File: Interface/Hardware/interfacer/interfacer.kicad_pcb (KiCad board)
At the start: 2 copper layers, 125.5 x 56.9 mm, 103 parts, among them J1 I2C, J10 5VDC barrel jack, J11 PWR, J12 5V, J13 GPS2 conn, J14 PPS direct, J15 PPS feedback, J16 DC/DC in, J17 5V isolated, J18 RJ45, J19 left top conn, J2 line UART, J20 right top conn, J3 GPS2 UART, J4 GPS1 UART, J5 PPS direct, J6 PPS selecctor, J7 PPS feedback, J8 left bottom conn, J9 right bottom conn, Q1 BSV52LT1G, Q2 BSV52LT1G, U1 ULN2003A, U2 LM92, U3 LM2940S-5.0, U4 L86, U5 NXJ1S0505MC, U6 ISO7421E, U7 ISO7421E, U8 SN65LBC179A, U9 SN65LBC179A

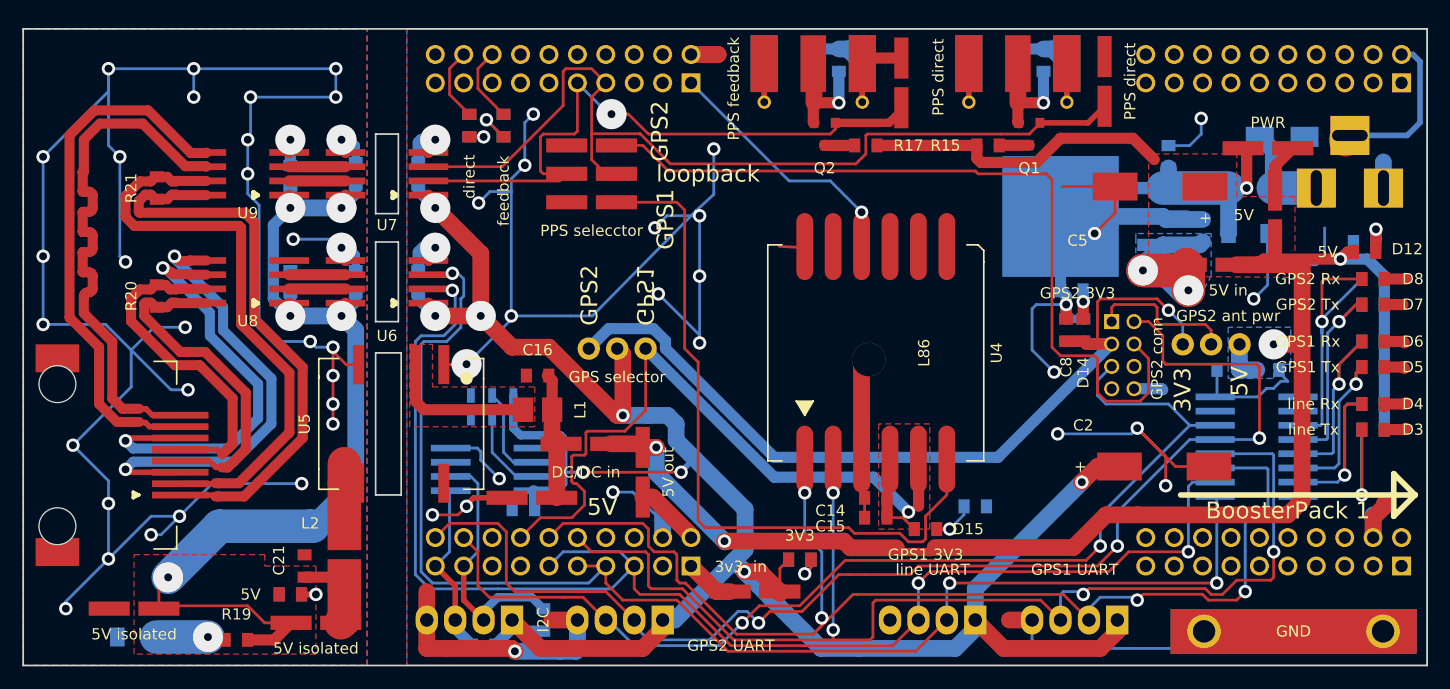
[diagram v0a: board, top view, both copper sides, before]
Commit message: silkscreen and solder mask finalization wiring touch-up
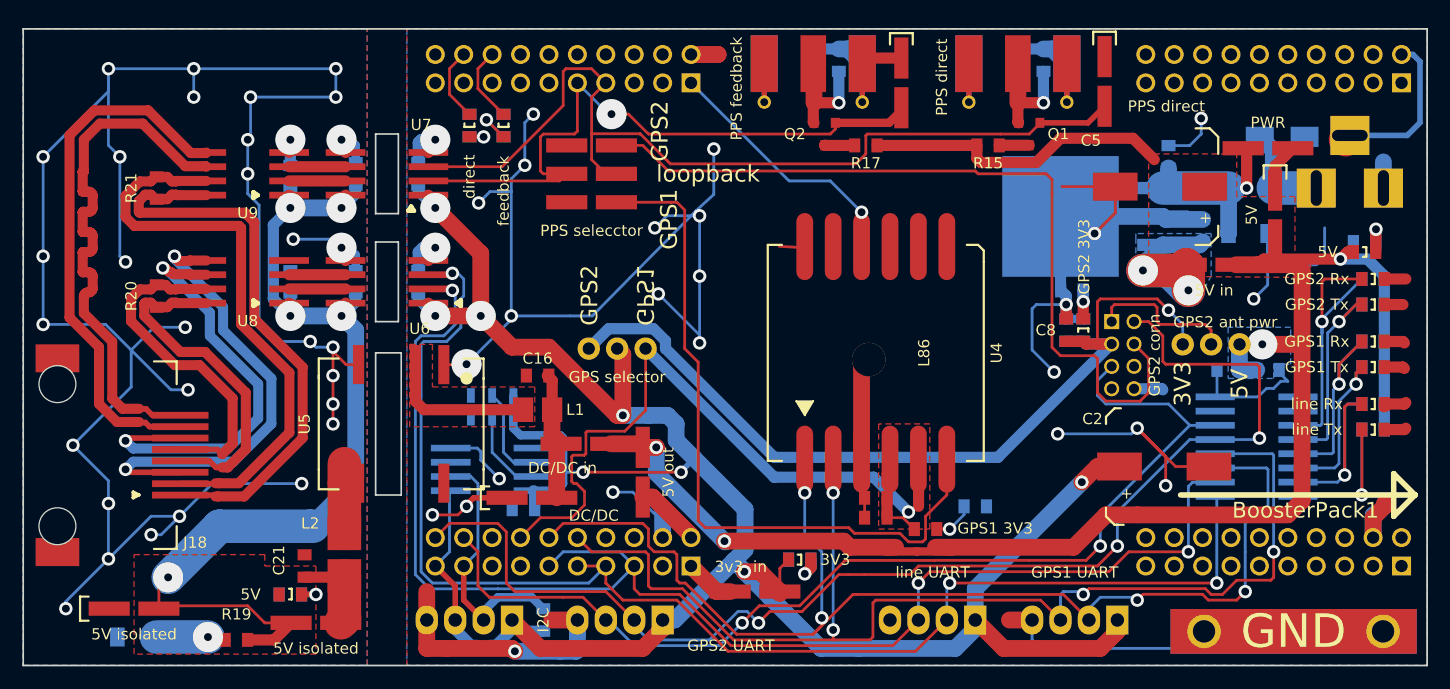
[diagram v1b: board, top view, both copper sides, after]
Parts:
- J16: value DC/DC in -> DC/DC
- J18: footprint auxiliary:8P8C_SMD -> 8P8C_SMD
- U4: footprint auxiliary:L86 -> L86
- moved R1 0.10 mm to (127.5, 125.3)
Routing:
- net +5V: track 157.3 -> 160.5 mm
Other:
- rule solder_mask_min_width: 0.16 -> 0.2
- board text added: "6.5V-20V"
- board text added: "BoosterPack1"
- board text removed: "BoosterPack 1"

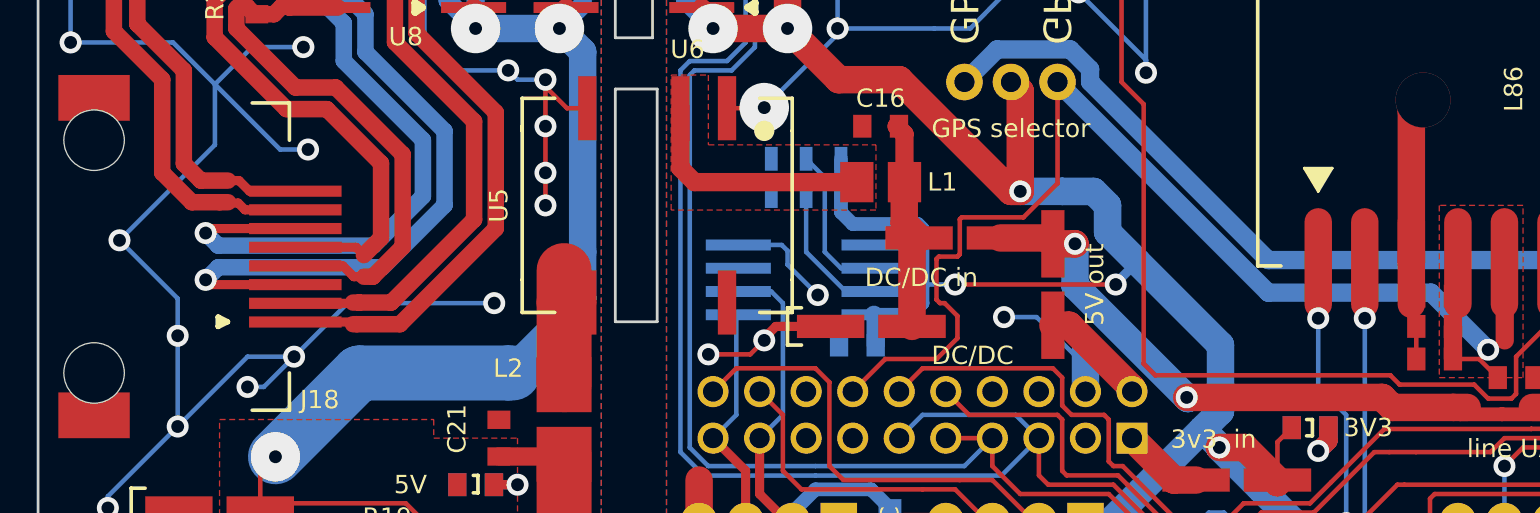
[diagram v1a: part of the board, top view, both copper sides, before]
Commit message: 8P8C, GPS1 gnd pin fix
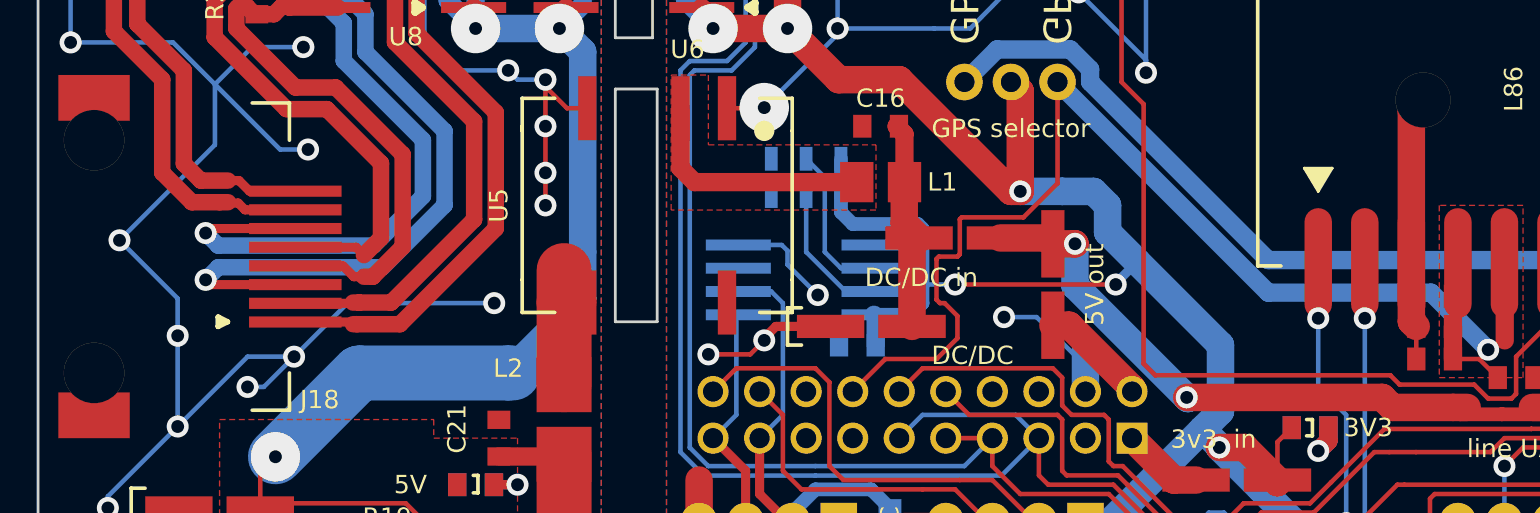
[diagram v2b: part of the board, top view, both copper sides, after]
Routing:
- net GND: track 396.2 -> 399.8 mm

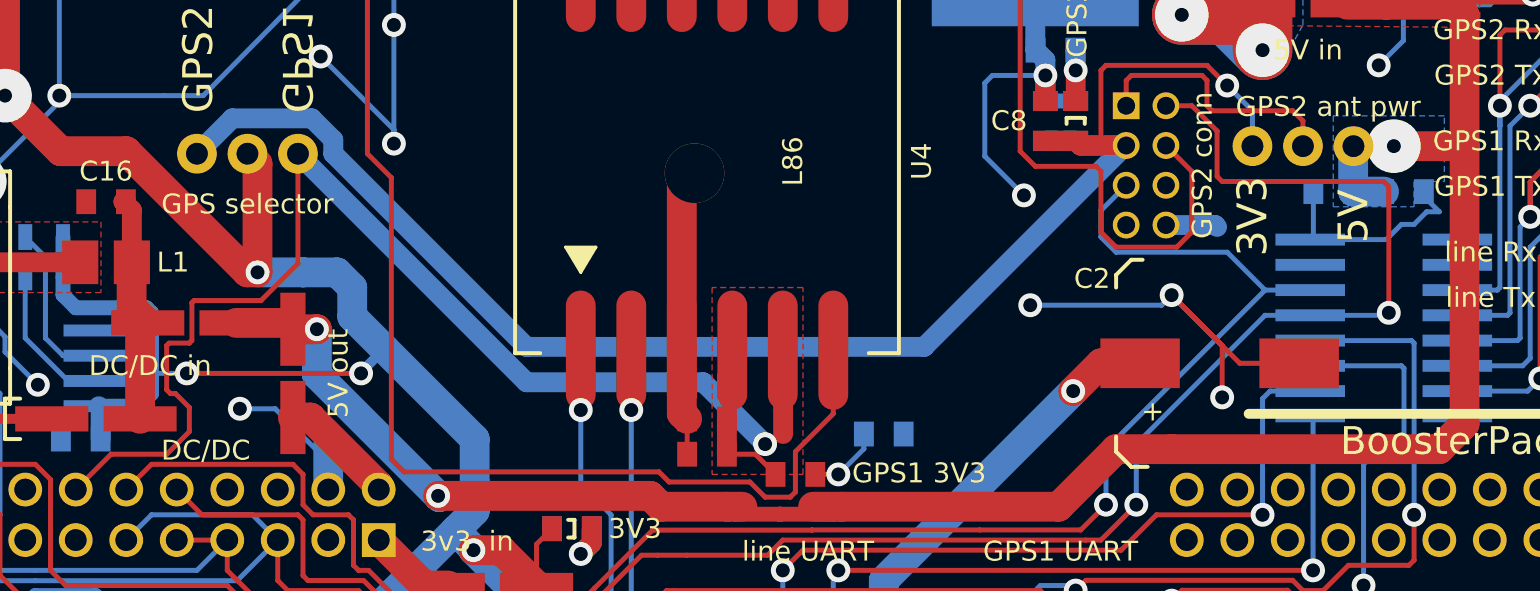
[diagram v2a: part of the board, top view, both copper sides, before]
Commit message: antenna power touch-up & green LED resistor value change
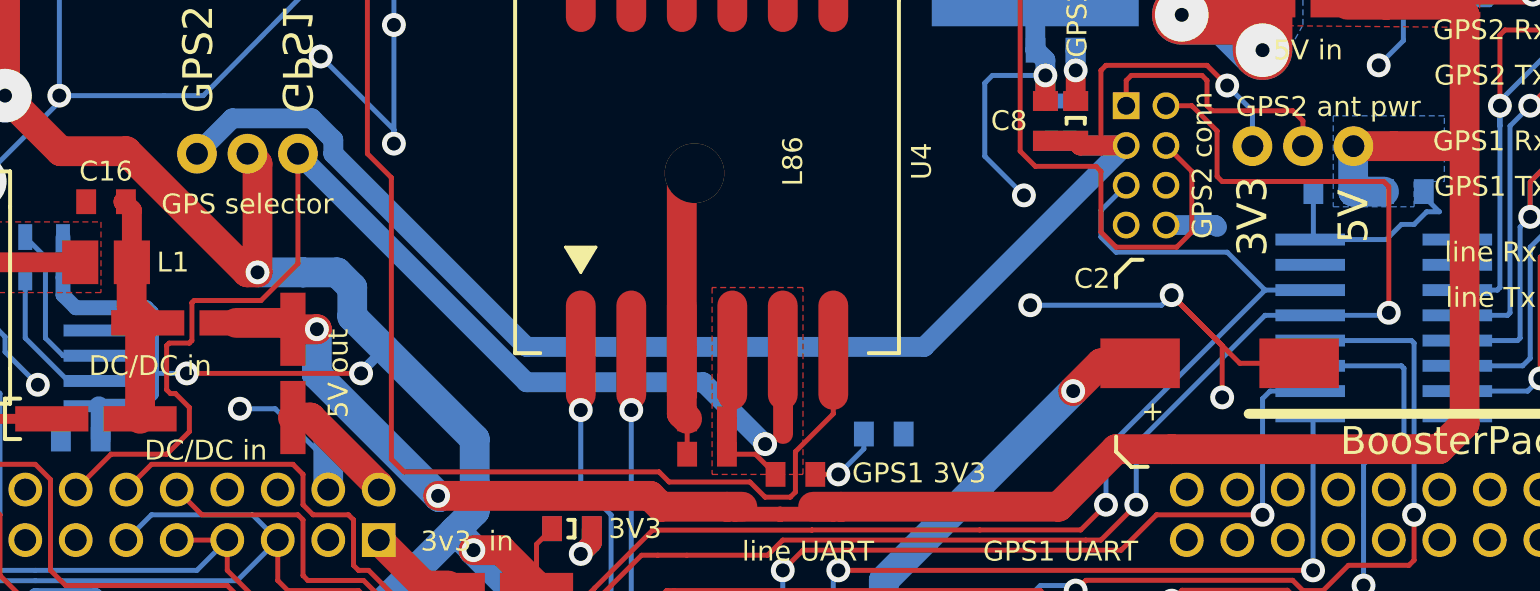
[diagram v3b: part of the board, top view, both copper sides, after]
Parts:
- J16: value DC/DC -> DC/DC in
- R5, R7, R9: value 1k5 -> 10k
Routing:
- net +5V: track 160.5 -> 162.5 mm, vias 4 -> 3
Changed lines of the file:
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@@
     (links 257)
     (no_connects 0)
-    (area 65.0113 49.7713 229.6287 151.6507)
+    (area 86.284999 70.028999 211.911001 127.075001)
     (thickness 1.55)
     (drawings 117)
@@
       (effects (font (size 1 1) (thickness 0.2)) (justify mirror))
     )
-    (fp_text value 1k5 (at 0 -0.127 180) (layer B.Fab)
+    (fp_text value 10k (at 0 -0.127 180) (layer B.Fab)
       (effects (font (size 1 1) (thickness 0.15)) (justify mirror))
     )
@@
       (effects (font (size 1 1) (thickness 0.2)) (justify mirror))
     )
-    (fp_text value 1k5 (at 0 0 180) (layer B.Fab)
+    (fp_text value 10k (at 0 0 180) (layer B.Fab)
       (effects (font (size 1 1) (thickness 0.15)) (justify mirror))
     )
@@
       (effects (font (size 1 1) (thickness 0.2)) (justify mirror))
     )
-    (fp_text value 1k5 (at 0 0.127 180) (layer B.Fab)
+    (fp_text value 10k (at 0 0.127 180) (layer B.Fab)
       (effects (font (size 1 1) (thickness 0.15)) (justify mirror))
     )
@@
       (effects (font (size 1 1) (thickness 0.15)))
     )
-    (fp_text value DC/DC (at -5.5245 -1.5875 180) (layer F.SilkS)
+    (fp_text value "DC/DC in" (at -5.5245 -1.5875 180) (layer F.SilkS)
       (effects (font (size 1 1) (thickness 0.2)))
     )
@@
   (segment (start 191.77 89.138) (end 191.5 89.408) (width 1.5) (layer B.Cu) (net 4))
   (segment (start 191.5 89.408) (end 188.22 89.408) (width 1.5) (layer B.Cu) (net 4))
+  (segment (start 195.072 98.298) (end 197.104 98.298) (width 1.5) (layer F.Cu) (net 5))
+  (segment (start 197.104 98.298) (end 200.66 98.298) (width 1.5) (layer F.Cu) (net 5))
   (segment (start 163.576 116.4336) (end 163.95192 116.80952) (width 0.75) (layer F.Cu) (net 5))
   (segment (start 163.95192 116.80952) (end 166.23792 116.80952) (width 0.75) (layer F.Cu) (net 5))
@@
   (segment (start 166.23792 116.80952) (end 166.23284 116.80444) (width 0.75) (layer F.Cu) (net 5))
   (segment (start 183.134 113.538) (end 180.2384 116.4336) (width 1.5) (layer F.Cu) (net 5))
+  (segment (start 185.928 113.538) (end 183.134 113.538) (width 1.5) (layer F.Cu) (net 5))
+  (segment (start 200.66 112.268) (end 200.66 98.298) (width 1.5) (layer F.Cu) (net 5))
+  (segment (start 199.39 113.538) (end 200.66 112.268) (width 1.5) (layer F.Cu) (net 5))
+  (segment (start 185.928 113.538) (end 199.39 113.538) (width 1.5) (layer F.Cu) (net 5))
   (segment (start 180.2384 116.4336) (end 169.30878 116.4336) (width 1.5) (layer F.Cu) (net 5))
   (segment (start 169.30878 116.4336) (end 167.894 116.4336) (width 1.5) (layer F.Cu) (net 5))
@@
   (segment (start 142.936 107.508) (end 142.9385 107.5055) (width 1.5) (layer F.Cu) (net 5))
   (via (at 142.9385 107.5055) (size 1.2) (drill 0.7) (layers F.Cu B.Cu) (net 5))
-  (segment (start 185.928 113.538) (end 199.39 113.538) (width 1.5) (layer F.Cu) (net 5))
-  (segment (start 199.39 113.538) (end 200.66 112.268) (width 1.5) (layer F.Cu) (net 5))
-  (segment (start 200.66 112.268) (end 200.66 98.298) (width 1.5) (layer F.Cu) (net 5))
-  (segment (start 185.928 113.538) (end 183.134 113.538) (width 1.5) (layer F.Cu) (net 5))
   (segment (start 141.732 107.508) (end 141.412 107.188) (width 1.5) (layer F.Cu) (net 5))
   (segment (start 141.412 107.188) (end 138.872 107.188) (width 1.5) (layer F.Cu) (net 5))
@@
   (segment (start 204.089 90.678) (end 197.231 90.678) (width 1) (layer F.Cu) (net 5))
   (via (at 204.089 90.678) (size 1.2) (drill 0.7) (layers F.Cu B.Cu) (net 5))
-  (segment (start 197.104 98.298) (end 200.66 98.298) (width 1.5) (layer F.Cu) (net 5))
-  (via (at 197.104 98.298) (size 2.7) (drill 0.7) (layers F.Cu B.Cu) (net 5))
   (segment (start 200.66 98.298) (end 200.66 91.694) (width 1.5) (layer F.Cu) (net 5))
-  (segment (start 200.66 91.694) (end 200.152 91.186) (width 1.5) (layer F.Cu) (net 5))
   (segment (start 200.152 91.186) (end 196.723 91.186) (width 1.5) (layer F.Cu) (net 5))
+  (segment (start 200.66 91.694) (end 200.152 91.186) (width 1.5) (layer F.Cu) (net 5))
   (segment (start 196.723 91.186) (end 194.752 91.186) (width 1.5) (layer F.Cu) (net 5))
   (segment (start 195.056 100.584) (end 196.612 100.584) (width 1.5) (layer B.Cu) (net 5))
